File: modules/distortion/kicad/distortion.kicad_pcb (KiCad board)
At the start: 2 copper layers, 136.4 x 80 mm, 57 parts, among them P1 CONN_01X03, P10 CONN_01X03, P11 CONN_01X03, P12 CONN_01X03, P13 CONN_01X03, P14 CONN_01X03, P2 CONN_01X03, P3 CONN_01X03, P4 CONN_01X03, P5 CONN_01X03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

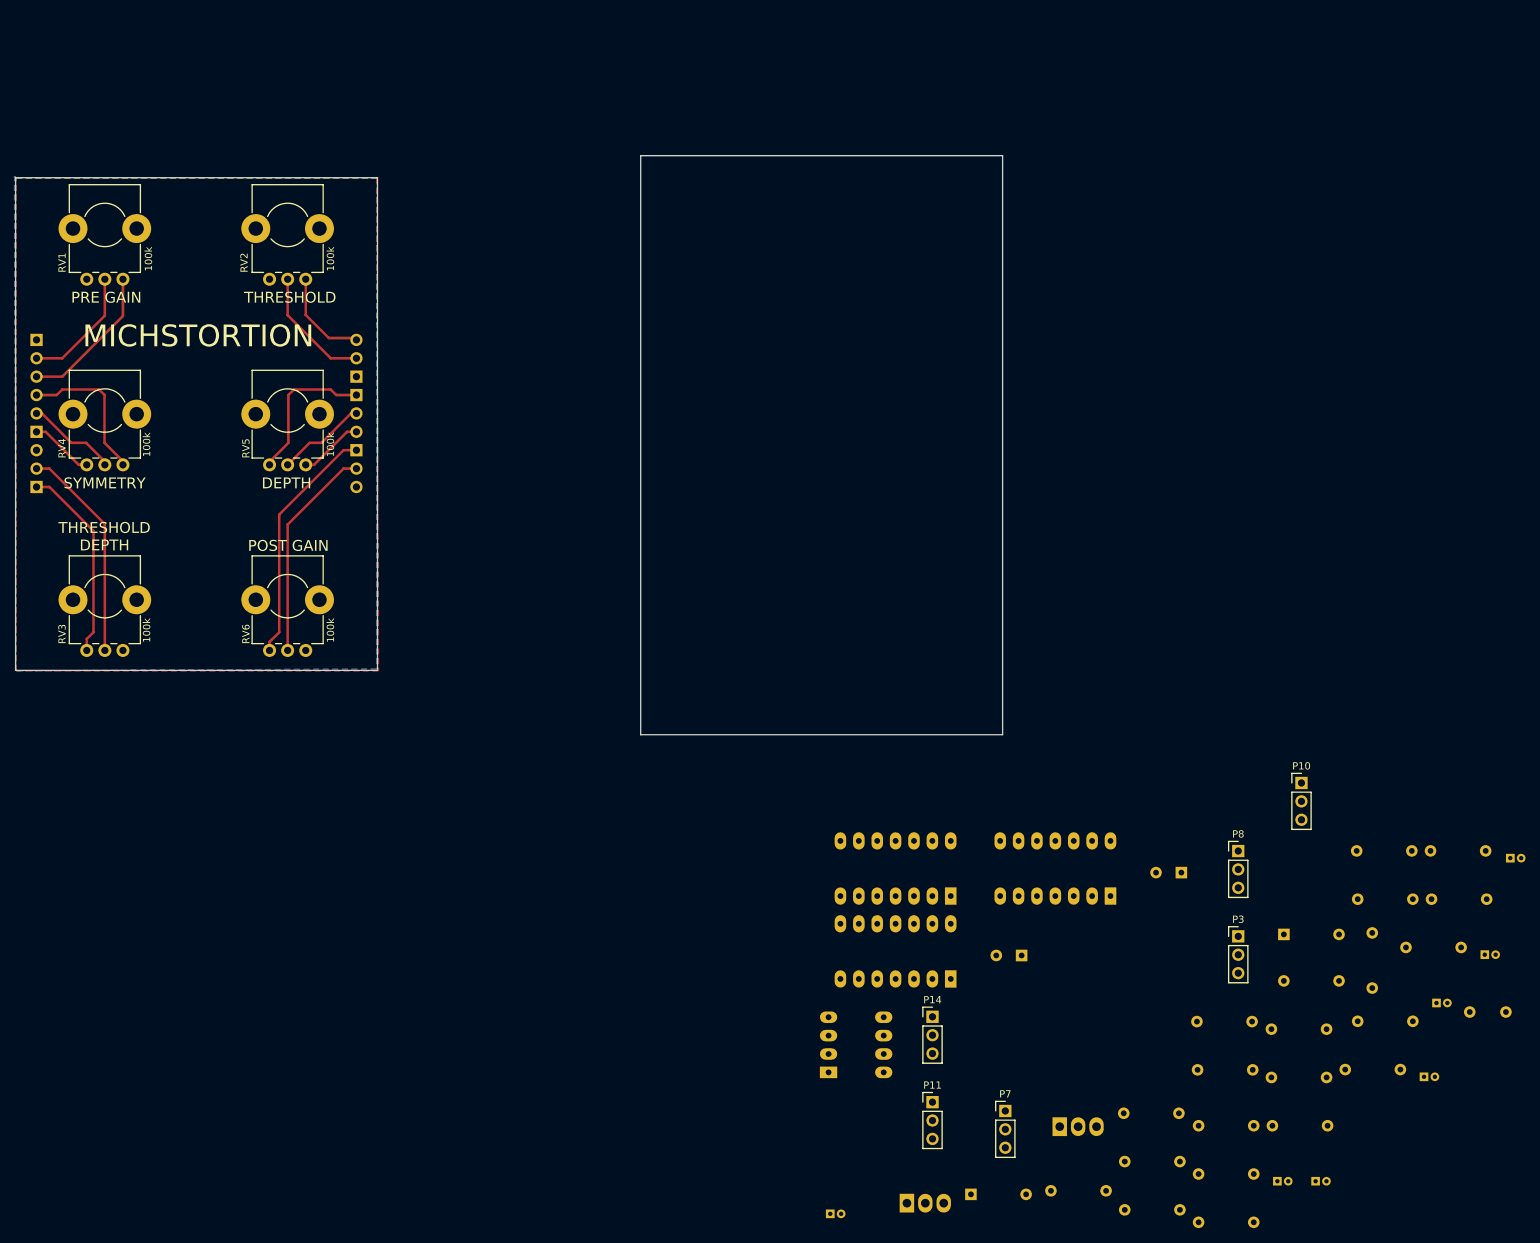
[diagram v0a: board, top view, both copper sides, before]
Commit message: Distortion pcb: panelization stuff, started layout wip
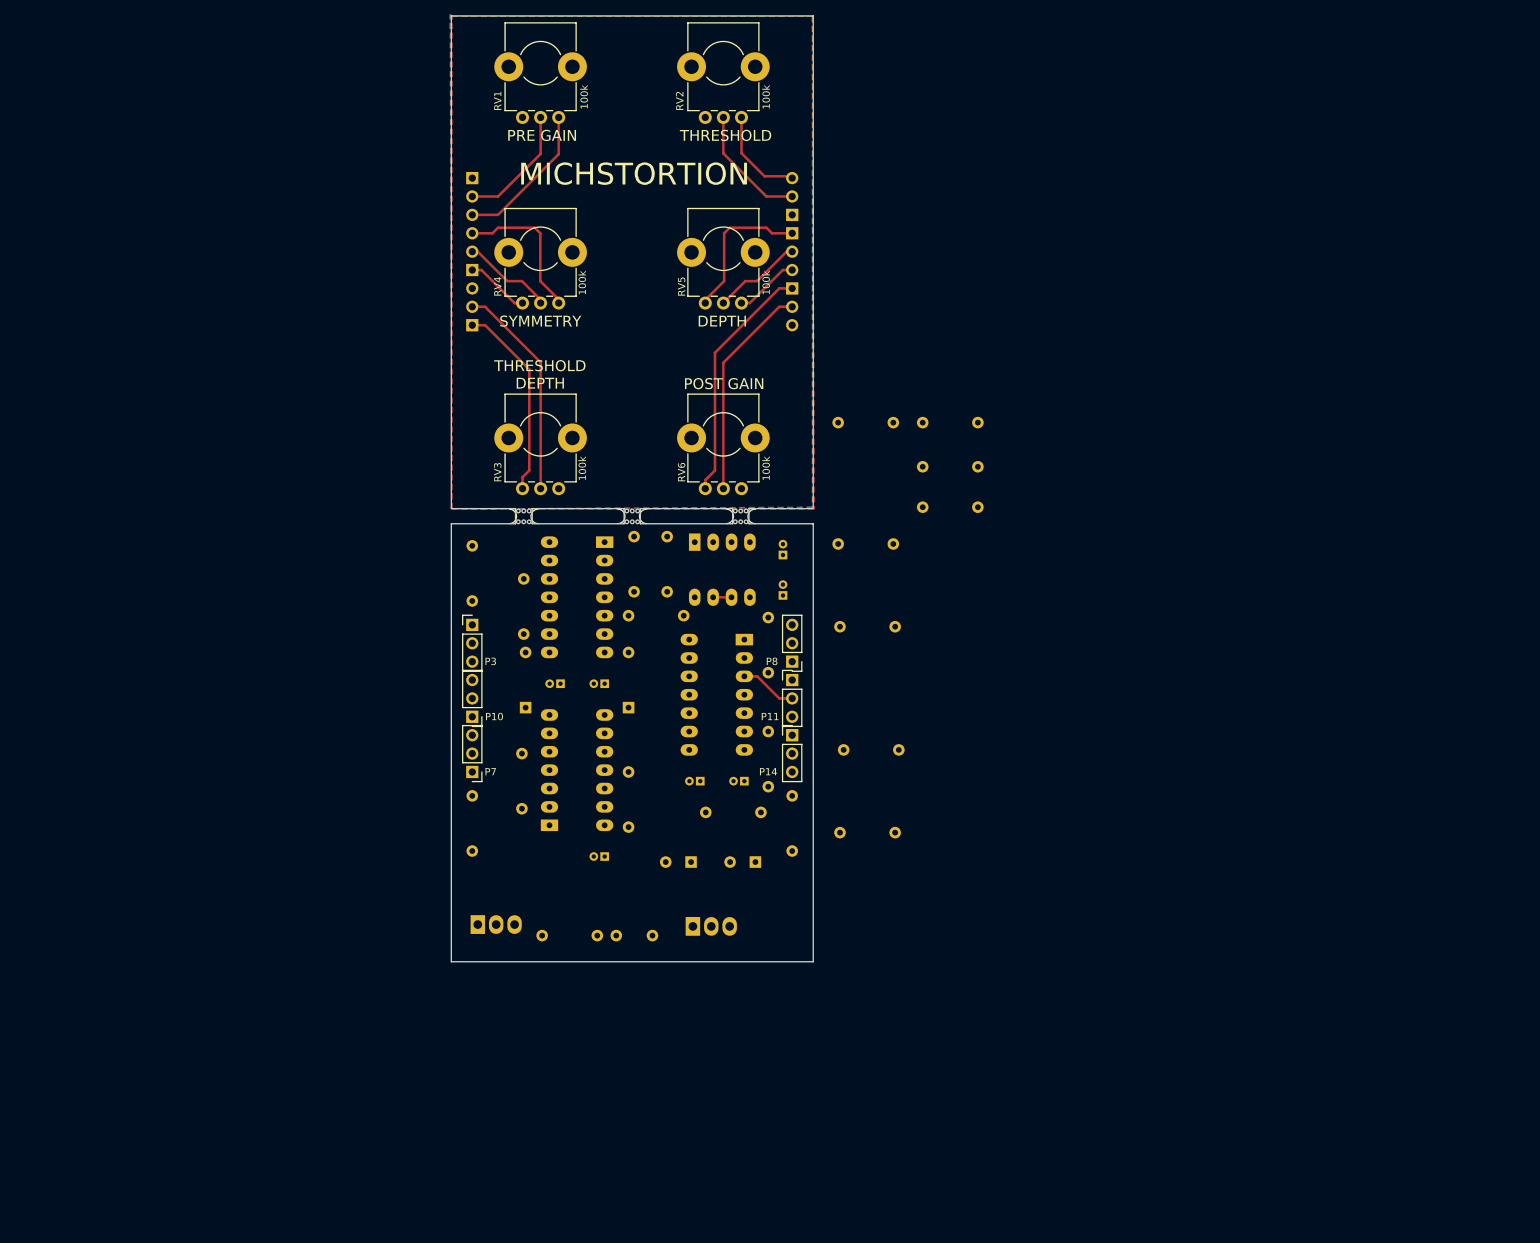
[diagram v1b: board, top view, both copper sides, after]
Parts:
- added mouse-bite-2mm-slot: VAL**, Panelization:mouse-bite-2mm-slot, F.Cu at (112.5, 93.5)
- added mouse-bite-2mm-slot: VAL**, Panelization:mouse-bite-2mm-slot, F.Cu at (97.5, 93.5)
- added mouse-bite-2mm-slot: VAL**, Panelization:mouse-bite-2mm-slot, F.Cu at (127.5, 93.5)
- moved R1 129.2 mm to (90.4, 97.5), turned to 270 degrees
- moved C5 123.1 mm to (108.7, 116.6), turned to 180 degrees
- moved C6 120.6 mm to (102.6, 116.6), turned to 180 degrees
- moved P10 114.9 mm to (90.4, 121.2), turned to 180 degrees
- moved P3 114.2 mm to (90.4, 108.5)
- moved C10 113.4 mm to (115.3, 151.4), turned to 180 degrees
- moved R5 111.8 mm to (112.8, 96.3), turned to 270 degrees
- moved R3 111.7 mm to (112.0, 107.2), turned to 0 degrees
- moved C4 111.6 mm to (133.3, 98.8), turned to 90 degrees
- moved R6 110.9 mm to (97.5, 109.7), turned to 90 degrees
- moved D2 109.3 mm to (97.8, 119.9), turned to 90 degrees
- moved R16 109.2 mm to (141.0, 80.5)
- moved C9 108.0 mm to (108.7, 140.5), turned to 180 degrees
- moved R2 107.7 mm to (117.3, 96.3), turned to 270 degrees
- moved C3 106.8 mm to (133.3, 104.4), turned to 90 degrees
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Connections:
- U3 pad 1: Net-(R15-Pad1) -> Net-(P14-Pad1)
- U3 pad 10: Net-(P11-Pad2) -> Net-(R14-Pad1)
- U3 pad 12: GND -> Net-(R12-Pad1)
- U3 pad 13: Net-(R19-Pad1) -> Net-(R11-Pad1)
- U3 pad 14: Net-(C10-Pad1) -> Net-(R15-Pad1)
- U3 pad 2: Net-(R11-Pad1) -> Net-(P14-Pad1)
- U3 pad 3: Net-(R12-Pad1) -> Net-(P11-Pad2)
- U3 pad 5: Net-(R14-Pad1) -> GND
- U3 pad 6: Net-(R13-Pad1) -> Net-(R19-Pad1)
- U3 pad 7: Net-(R16-Pad1) -> Net-(C10-Pad1)
- U3 pad 8: Net-(P14-Pad1) -> Net-(R16-Pad1)
- U3 pad 9: Net-(P14-Pad1) -> Net-(R13-Pad1)
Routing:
- net Net-(P11-Pad2): track 0.00 -> 7.87 mm
- net Net-(U1-Pad6): track 0.00 -> 2.54 mm
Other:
- board size 136.4 x 80 mm -> 50 x 130.7 mm

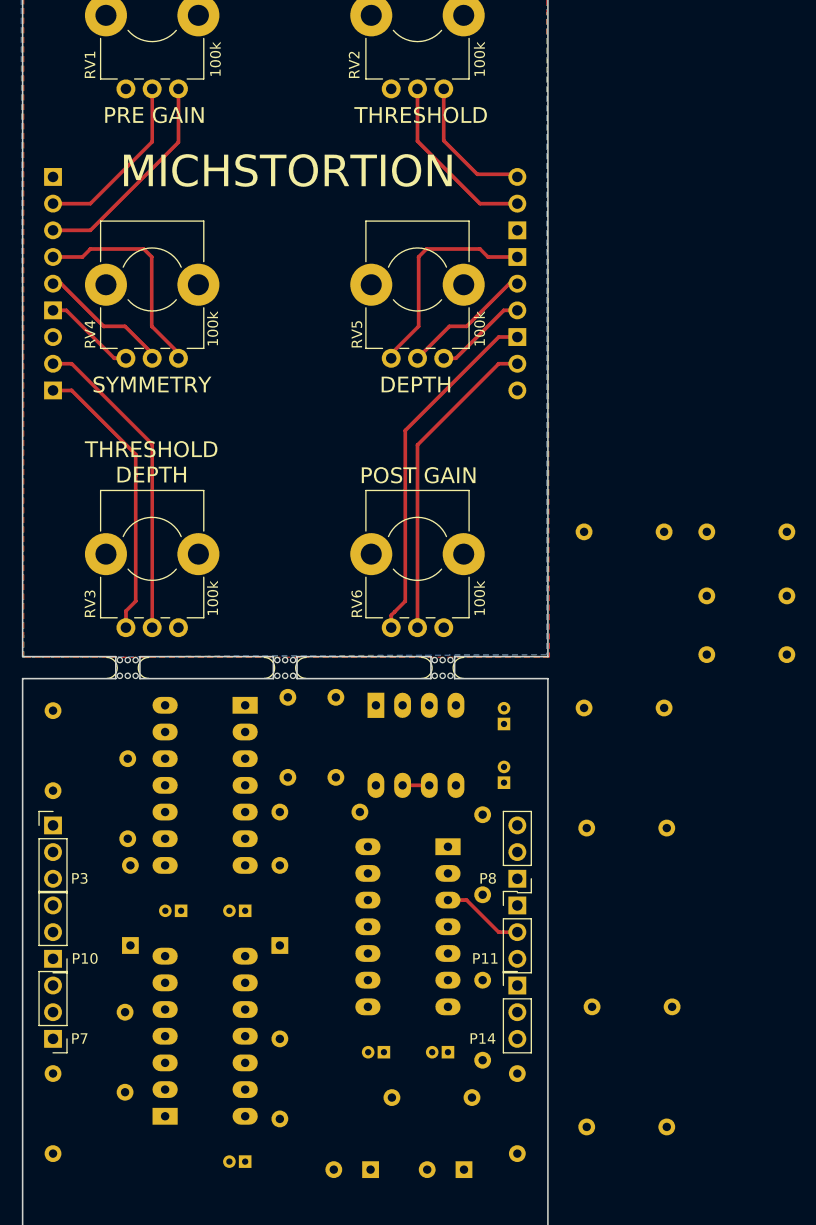
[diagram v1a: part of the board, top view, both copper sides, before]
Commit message: Distortion: move some resistors to top board WIP
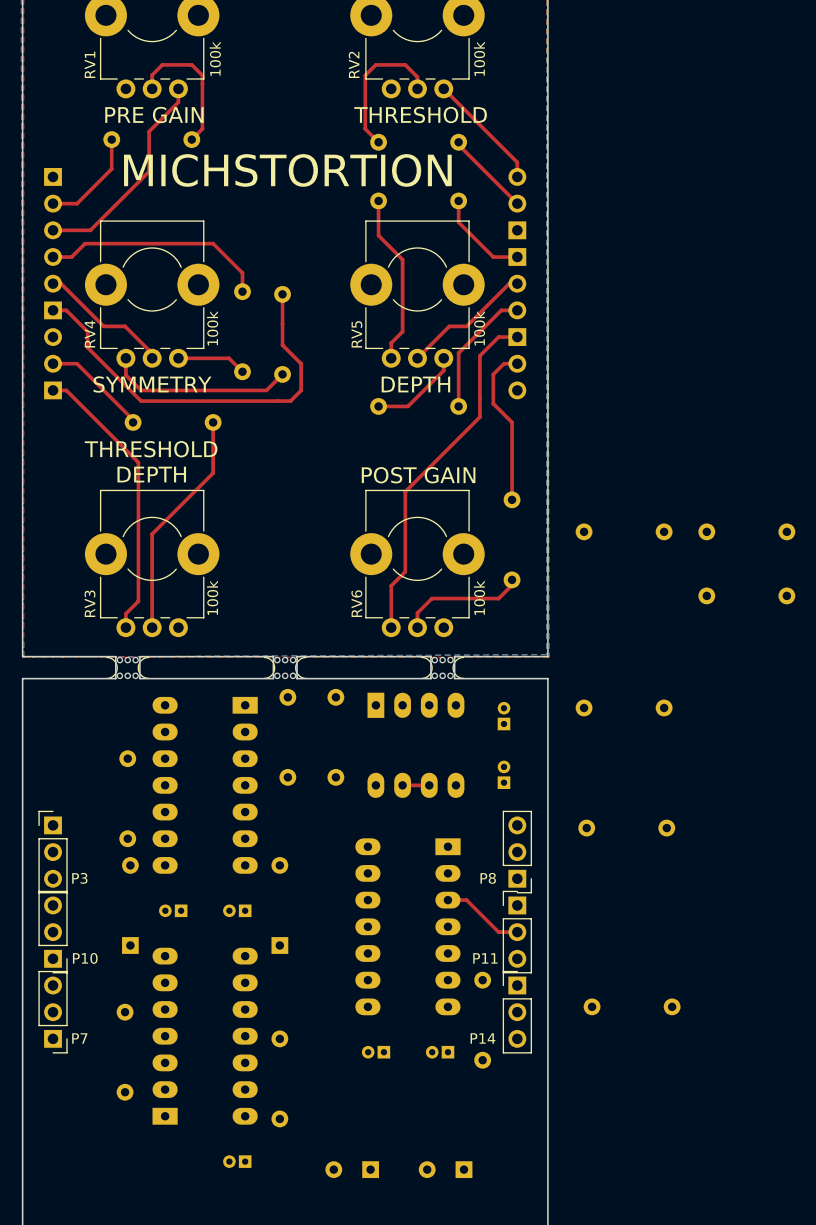
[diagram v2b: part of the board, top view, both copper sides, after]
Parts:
- moved R11 84.4 mm to (112.3, 57.9), turned to 270 degrees
- moved R4 70.0 mm to (98.0, 70.1), turned to 0 degrees
- moved R18 66.1 mm to (129.0, 49.0), turned to 180 degrees
- moved R3 66.0 mm to (129.0, 43.4), turned to 180 degrees
- moved R17 65.8 mm to (129.0, 68.6)
- moved R19 62.2 mm to (134.1, 77.5), turned to 270 degrees
- moved R13 56.1 mm to (108.5, 57.7), turned to 270 degrees
- moved R1 54.6 mm to (96.0, 43.2), turned to 0 degrees
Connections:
- P11 pad 1: Net-(P11-Pad1) -> Net-(P10-Pad2)
- P8 pad 2: Net-(P8-Pad2) -> Net-(P7-Pad2)
- R1 pad 1: Net-(R1-Pad1) -> Net-(P4-Pad2)
- R1 pad 2: Net-(P3-Pad2) -> Net-(R1-Pad2)
- R11 pad 1: Net-(R11-Pad1) -> Net-(P9-Pad1)
- R11 pad 2: Net-(P10-Pad1) -> Net-(R11-Pad2)
- R13 pad 1: Net-(R13-Pad1) -> Net-(P9-Pad3)
- R13 pad 2: Net-(P10-Pad3) -> Net-(R13-Pad2)
- R15 pad 2: Net-(R11-Pad1) -> Net-(P10-Pad1)
- R16 pad 2: Net-(R13-Pad1) -> Net-(P10-Pad3)
- R17 pad 1: Net-(P11-Pad3) -> Net-(P13-Pad3)
- R18 pad 1: Net-(P11-Pad1) -> Net-(P13-Pad1)
- R18 pad 2: Net-(P10-Pad2) -> Net-(R18-Pad2)
- R19 pad 1: Net-(R19-Pad1) -> Net-(P12-Pad2)
- R19 pad 2: Net-(P14-Pad2) -> Net-(R19-Pad2)
- R2 pad 2: Net-(R1-Pad1) -> Net-(P3-Pad2)
- R20 pad 2: Net-(R19-Pad1) -> Net-(P14-Pad2)
- R3 pad 1: Net-(R3-Pad1) -> Net-(P6-Pad2)
- R3 pad 2: Net-(P8-Pad2) -> Net-(R3-Pad2)
- R4 pad 1: Net-(R3-Pad1) -> Net-(P5-Pad2)
- R4 pad 2: Net-(P7-Pad2) -> Net-(R4-Pad2)
- R5 pad 2: Net-(R3-Pad1) -> Net-(P7-Pad2)
- RV1 pad 2: Net-(P4-Pad2) -> Net-(R1-Pad2)
- RV2 pad 2: Net-(P6-Pad2) -> Net-(R3-Pad2)
- RV3 pad 2: Net-(P5-Pad2) -> Net-(R4-Pad2)
- RV4 pad 1: Net-(P9-Pad3) -> Net-(R13-Pad2)
- RV4 pad 3: Net-(P9-Pad1) -> Net-(R11-Pad2)
- RV5 pad 1: Net-(P13-Pad3) -> Net-(R17-Pad2)
- RV5 pad 3: Net-(P13-Pad1) -> Net-(R18-Pad2)
- RV6 pad 2: Net-(P12-Pad2) -> Net-(R19-Pad2)
- U1 pad 2: Net-(R1-Pad1) -> Net-(P3-Pad2)
- U2 pad 2: Net-(R3-Pad1) -> Net-(P7-Pad2)
- U3 pad 13: Net-(R11-Pad1) -> Net-(P10-Pad1)
- U3 pad 6: Net-(R19-Pad1) -> Net-(P14-Pad2)
- U3 pad 9: Net-(R13-Pad1) -> Net-(P10-Pad3)
- U4 pad 2: Net-(R17-Pad2) -> Net-(P11-Pad3)
- U4 pad 3: Net-(R17-Pad2) -> Net-(P11-Pad3)
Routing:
- net Net-(P9-Pad1): track 8.83 -> 38.4 mm
- net Net-(R4-Pad2): track 0.00 -> 21.9 mm
- net Net-(P5-Pad2): track 30.1 -> 10.1 mm
- net Net-(R11-Pad2): track 0.00 -> 17.8 mm
- net Net-(R18-Pad2): track 0.00 -> 16.8 mm
- net Net-(P12-Pad2): track 30.1 -> 15.4 mm
- net Net-(R3-Pad2): track 0.00 -> 13.9 mm
- net Net-(R1-Pad2): track 0.00 -> 13.4 mm
- net Net-(R19-Pad2): track 0.00 -> 12.0 mm
- net Net-(P13-Pad1): track 20.7 -> 8.99 mm
- net Net-(R17-Pad2): track 0.00 -> 9.87 mm
- net Net-(P6-Pad2): track 16.9 -> 8.16 mm
- net Net-(P4-Pad2): track 16.9 -> 9.75 mm
- net Net-(R13-Pad2): track 0.00 -> 7.14 mm
- net Net-(P13-Pad3): track 8.89 -> 12.6 mm
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
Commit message: Distortion: finishing routing pcb and silkscreen
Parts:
- moved R8 61.6 mm to (94.2, 106.2), turned to 90 degrees
- moved R16 60.3 mm to (118.4, 136.4), turned to 90 degrees
- moved R15 43.6 mm to (122.2, 111.8)
- moved R7 41.4 mm to (101.1, 98.6)
- moved R12 34.7 mm to (116.3, 121.7), turned to 90 degrees
- moved R14 27.4 mm to (115.1, 132.1), turned to 90 degrees
- moved R20 12.0 mm to (134.9, 142.2)
- moved U3 5.14 mm to (129.8, 115.3)
- moved C7 5.14 mm to (129.8, 134.9)
- moved C8 5.14 mm to (123.7, 134.9)
- moved C9 5.08 mm to (108.7, 145.5)
- moved R10 5.08 mm to (97.3, 131.3)
- moved R6 5.08 mm to (97.5, 114.8)
- moved R9 5.08 mm to (112.0, 141.5)
- moved C5 5.08 mm to (108.7, 121.7)
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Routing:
- net VCC: track 0.00 -> 132.0 mm, vias 0 -> 1
- net VEE: track 0.00 -> 123.3 mm, vias 0 -> 1
- net Net-(P10-Pad2): track 0.00 -> 98.9 mm
- net Net-(P10-Pad1): track 0.00 -> 90.9 mm, vias 0 -> 1
- net Net-(P11-Pad3): track 0.00 -> 74.5 mm, vias 0 -> 3
- net Net-(P7-Pad2): track 0.00 -> 74.2 mm, vias 0 -> 4
- net Net-(R15-Pad1): track 0.00 -> 72.1 mm, vias 0 -> 4
- net SignalIn: track 0.00 -> 60.3 mm
- net Net-(P3-Pad2): track 0.00 -> 54.2 mm
- net Net-(R16-Pad1): track 0.00 -> 47.4 mm, vias 0 -> 3
- net Net-(R14-Pad2): track 0.00 -> 46.7 mm
- net Net-(R12-Pad2): track 0.00 -> 45.5 mm
- net Net-(C10-Pad1): track 0.00 -> 44.5 mm
- net Net-(P10-Pad3): track 0.00 -> 38.2 mm, vias 0 -> 2
- net ThresholdIn: track 0.00 -> 22.4 mm
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- added copper zone on B.Cu, net GND
- added copper zone on F.Cu, net GND
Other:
- board size 50 x 130.7 mm -> 50 x 132.2 mm
- board text added: "+5V"
- board text added: "-5V"
- board text added: "0V"
- board text added: "BOARD 1/2"
- board text added: "BOARD 2/2"
- board text added: "IN"
- board text added: "MICH'S FOLDBACK DISTORTION MICHD, AUGUST 2017"
- board text added: "OUT"
- board text added: "POWER"
- board text added: "THRSH"
